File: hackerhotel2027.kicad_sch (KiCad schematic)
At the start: 371 parts, among them J1 USB device, J2 Battery, J3 Debug, Q1 JSM2301S, SW1 TS-1187A-B-A-B, SW2 TS-1187A-B-A-B, SW3 TS-1187A-B-A-B, SW4 TS-1187A-B-A-B, U1 CH643Q, U2 TPD4E05U06DQAR, U3 XT4054K421MR-G

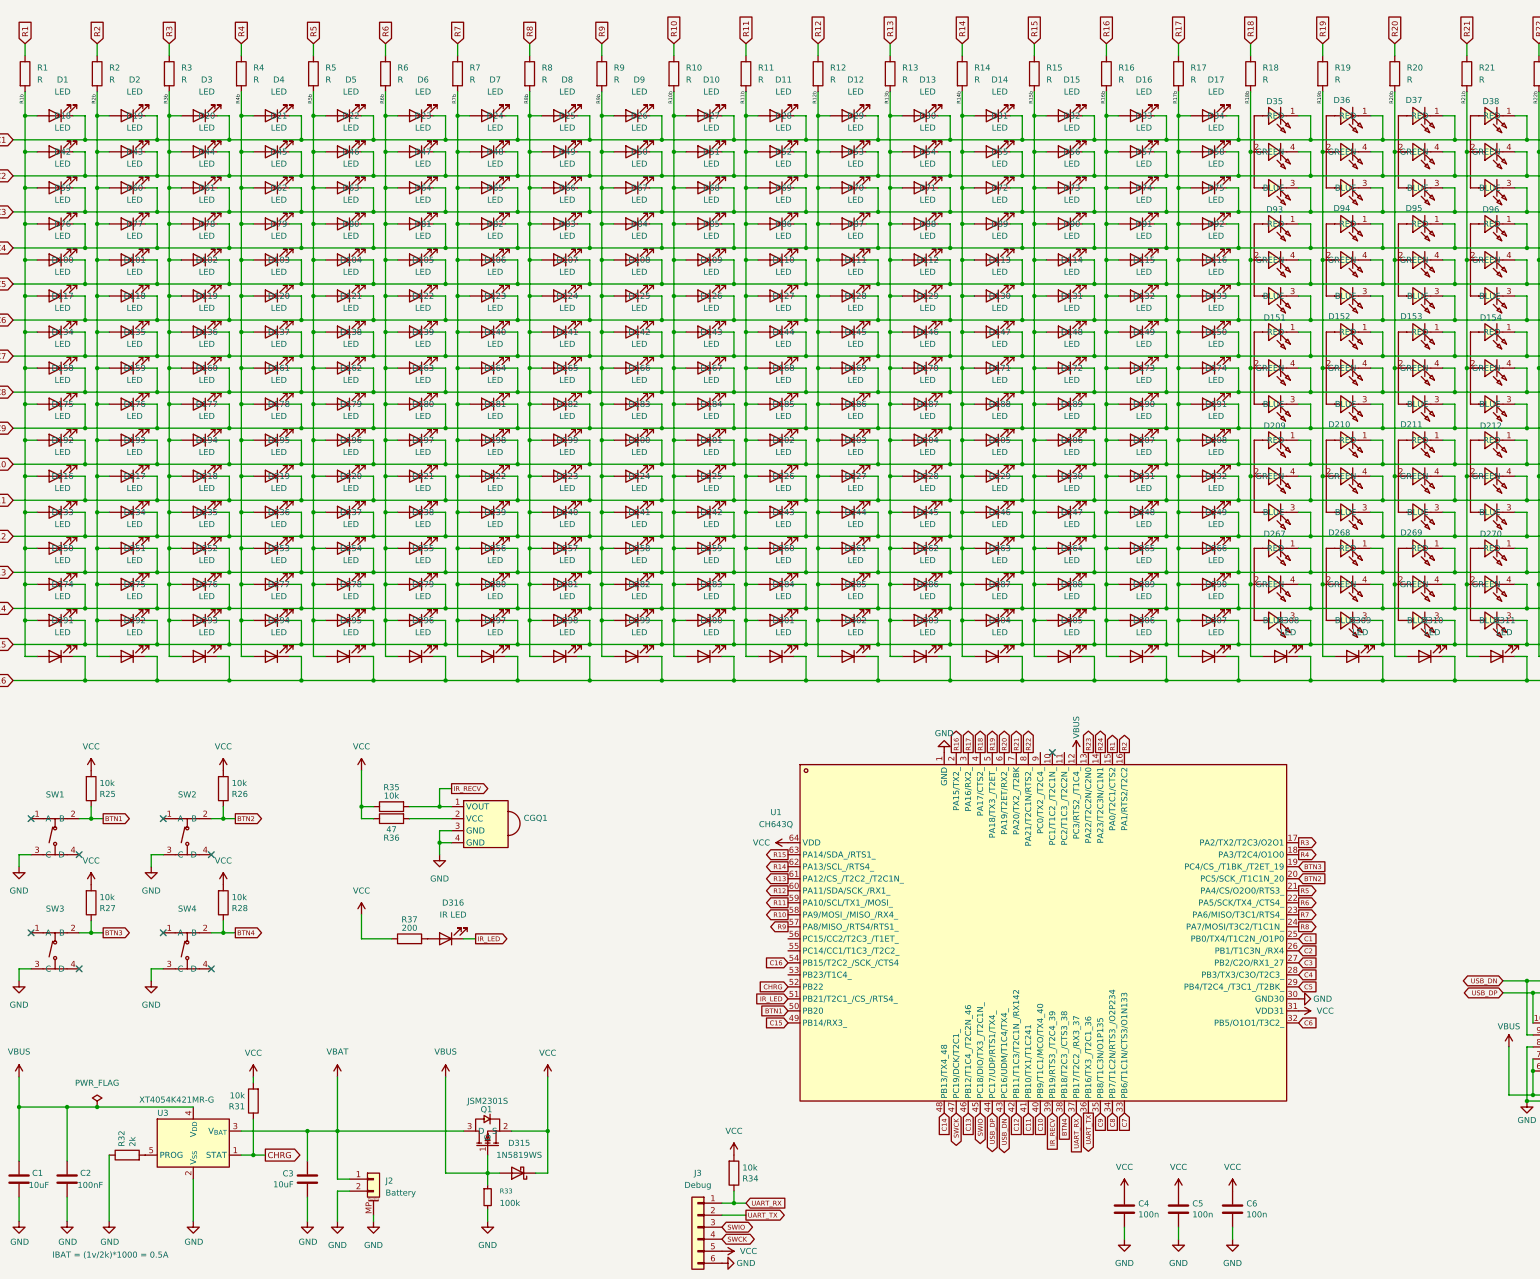
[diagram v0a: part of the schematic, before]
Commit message: (temporarily) removed some LEDs, changed to 6 layer board, 0 unrouted, no DRC errors
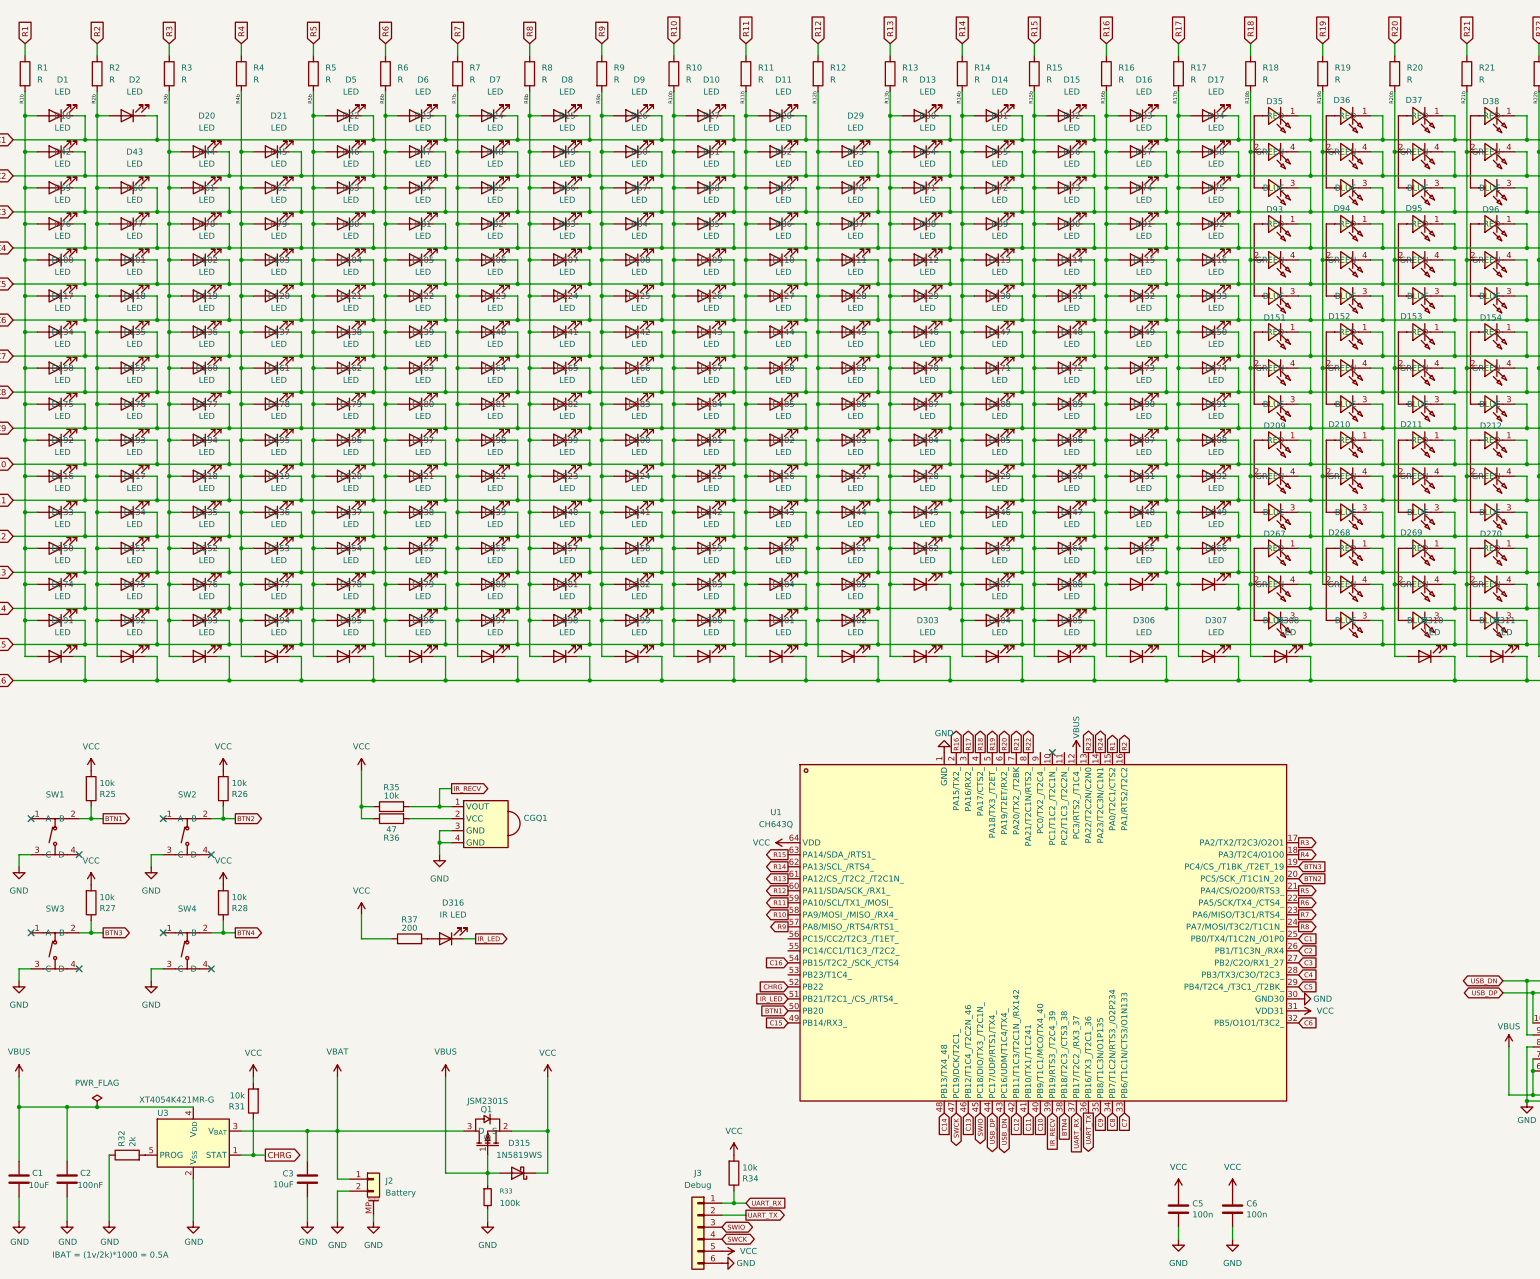
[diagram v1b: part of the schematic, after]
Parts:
- removed C4: 100n, Capacitor_SMD:C_0402_1005Metric, symbol symbols:C
- removed D12, D19, D286, D289, D290, D3, D309, D4: LED, LED_SMD:LED_0402_1005Metric, symbol Device:LED

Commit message: The final push (from me for prototype 1 :P)
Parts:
- added D12, D19, D286, D289, D290, D3, D309, D4: LED, LED_SMD:LED_0402_1005Metric, symbol Device:LED
- added N1: Badge.Team stamp, badgeteam:stamp_small, symbol Mechanical:Housing
- renumbered C5 to C4, C6 to C5, D316 to D315, D315 to D316, R35 to R27, R36 to R28, R27 to R29, R28 to R30, R29 to R31, R37 to R32, R30 to R33, R31 to R34, R32 to R35, R34 to R36, R33 to R37
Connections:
- net C1: now also D12.1 (K), D3.1 (K), D4.1 (K)
- net C15: now also D286.1 (K), D289.1 (K), D290.1 (K)
- net C16: now also D309.1 (K)
- net C2: now also D19.1 (K)
- net R12b: now also D12.2 (A)
- net R13b: now also D286.2 (A)
- net R16b: now also D289.2 (A)
- net R17b: now also D290.2 (A)
- net R19b: now also D309.2 (A)
- net R2b: now also D19.2 (A)
- net R3b: now also D3.2 (A)
- net R4b: now also D4.2 (A)
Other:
- company: (none) -> Badge.Team
- title: (none) -> Hackerhotel 2027 badge

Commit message: Some cleanup on the PCB.
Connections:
- no-connect marks 11 -> 16
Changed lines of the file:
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@@
+	)
+	(no_connect
+		(at 191.77 210.82)
 	)
 	(no_connect
@@
 	)
 	(no_connect
+		(at 250.19 171.45)
+	)
+	(no_connect
+		(at 191.77 213.36)
+	)
+	(no_connect
 		(at 59.69 209.55)
+	)
+	(no_connect
+		(at 245.11 171.45)
 	)
 	(no_connect
@@
 	)
 	(no_connect
+		(at 191.77 218.44)
+	)
+	(no_connect

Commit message: Prototype 1
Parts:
- added C7: 10u, Capacitor_SMD:C_0603_1608Metric, symbol symbols:C
- added C8: 1u, Capacitor_SMD:C_0603_1608Metric, symbol mch2021-rescue:C-Device
- C3: value 10uF -> 10u
- D1, D10, D100, D101, D102, D103, D104, D105, D106, D107, D108, D109, D11, D110, D111, D112, D113, D114, D115, D116, D117, D118, D119, D12, D120, D121, D122, D123, D124, D125, D126, D127, D128, D129, D13, D130, D131, D132, D133, D134, D135, D136, D137, D138, D139, D14, D140, D141, D142, D143, D144, D145, D146, D147, D148, D149, D15, D150, D158, D159, D16, D160, D161, D162, D163, D164, D165, D166, D167, D168, D169, D17, D170, D171, D172, D173, D174, D175, D176, D177, D178, D179, D18, D180, D181, D182, D183, D184, D185, D186, D187, D188, D189, D19, D190, D191, D192, D193, D194, D195, D196, D197, D198, D199, D2, D20, D200, D201, D202, D203, D204, D205, D206, D207, D208, D21, D216, D217, D218, D219, D22, D220, D221, D222, D223, D224, D225, D226, D227, D228, D229, D23, D230, D231, D232, D233, D234, D235, D236, D237, D238, D239, D24, D240, D241, D242, D243, D244, D245, D246, D247, D248, D249, D25, D250, D251, D252, D253, D254, D255, D256, D257, D258, D259, D26, D260, D261, D262, D263, D264, D265, D266, D27, D274, D275, D276, D277, D278, D279, D28, D280, D281, D282, D283, D284, D285, D286, D287, D288, D289, D29, D290, D291, D292, D293, D294, D295, D296, D297, D298, D299, D3, D30, D300, D301, D302, D303, D304, D305, D306, D307, D308, D309, D31, D310, D311, D312, D313, D314, D32, D33, D34, D4, D42, D43, D44, D45, D46, D47, D48, D49, D5, D50, D51, D52, D53, D54, D55, D56, D57, D58, D59, D6, D60, D61, D62, D63, D64, D65, D66, D67, D68, D69, D7, D70, D71, D72, D73, D74, D75, D76, D77, D78, D79, D8, D80, D81, D82, D83, D84, D85, D86, D87, D88, D89, D9, D90, D91, D92: footprint LED_SMD:LED_0402_1005Metric -> led_no_silk:LED_0402_1005Metric_nosilk
- J3, N1: LCSC Part (none) -> -; now left out of the parts list
- R1, R10, R11, R12, R13, R14, R15, R16, R17, R18, R19, R2, R20, R21, R22, R23, R24, R3, R4, R5, R6, R7, R8, R9: value R -> 200; LCSC Part (none) -> C25087
- R32: LCSC Part (none) -> C25087
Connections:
- net GND: now also C7.2, C8.2
- net VCC: now also C7.1, C8.1
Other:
- moved on the sheet: J2

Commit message: Prototype 1 (production)
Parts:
- C1: value 10uF -> 10u
- C2: value 100nF -> 100n
- C8: LCSC C5199872 -> (none); LCSC Part C107372 -> C5199872
- D315, J2: FT Rotation Offset (none) -> 180
- Q1: FT Rotation Offset 180 -> 0
- U1, U2: FT Rotation Offset (none) -> 90
- U3: FT Rotation Offset 180 -> 90
- renumbered CGQ1 to S1
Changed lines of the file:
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@@
 			)
 		)
-		(property "FT Rotation Offset" "180"
+		(property "FT Rotation Offset" "0"
 			(at 128.27 251.46 0)
 			(hide yes)
@@
 			)
 		)
-		(property "Value" "100nF"
+		(property "Value" "100n"
 			(at 46.99 262.89 0)
 			(show_name no)
@@
 			)
 		)
-		(property "FT Rotation Offset" ""
+		(property "FT Rotation Offset" "90"
 			(at 359.41 233.68 0)
 			(hide yes)
@@
 			)
 		)
+		(property "FT Rotation Offset" "180"
+			(at 116.84 261.62 0)
+			(hide yes)
+			(show_name no)
+			(do_not_autoplace no)
+			(effects
+				(font
+					(size 1.27 1.27)
+				)
+			)
+		)
 		(pin "1"
 		)
@@
 			)
 		)
-		(property "FT Rotation Offset" ""
+		(property "FT Rotation Offset" "180"
 			(at 119.38 210.82 0)
 			(hide yes)
@@
 			)
 		)
-		(property "LCSC" "C5199872"
+		(property "LCSC" ""
 			(at 154.94 261.62 0)
 			(hide yes)
@@
 			)
 		)
-		(property "LCSC Part" "C107372"
+		(property "LCSC Part" "C5199872"
 			(at 154.94 261.62 0)
 			(hide yes)
@@
 			)
 		)
-		(property "Value" "10uF"
+		(property "Value" "10u"
 			(at 35.56 262.89 0)
 			(show_name no)
@@
 		(dnp no)
 		(fields_autoplaced yes)
-		(property "Reference" "CGQ1"
+		(property "Reference" "S1"
 			(at 135.89 185.2949 0)
 			(show_name no)
@@
 			(project "hackerhotel2027"
 				(path "/0ab9a1db-7560-4118-92b8-33ec87c3cf01"
-					(reference "CGQ1")
+					(reference "S1")
 					(unit 1)
 				)
@@
 			)
 		)
-		(property "FT Rotation Offset" "180"
+		(property "FT Rotation Offset" "90"
 			(at 66.04 254 0)
 			(hide yes)
@@
 			)
 		)
-		(property "FT Rotation Offset" ""
+		(property "FT Rotation Offset" "90"
 			(at 245.11 209.55 90)
 			(hide yes)

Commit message: Different battery connector
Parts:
- J2: footprint Connector_JST:JST_PH_B2B-PH-SM4-TB_1x02-1MP_P2.00mm_Vertical -> jst:CONN-SMD_PH-2AWB
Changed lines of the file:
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@@
 			)
 		)
-		(property "Footprint" "Connector_JST:JST_PH_B2B-PH-SM4-TB_1x02-1MP_P2.00mm_Vertical"
+		(property "Footprint" "jst:CONN-SMD_PH-2AWB"
 			(at 116.84 261.62 0)
 			(hide yes)
